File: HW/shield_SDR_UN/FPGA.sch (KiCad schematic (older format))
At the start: 34 parts

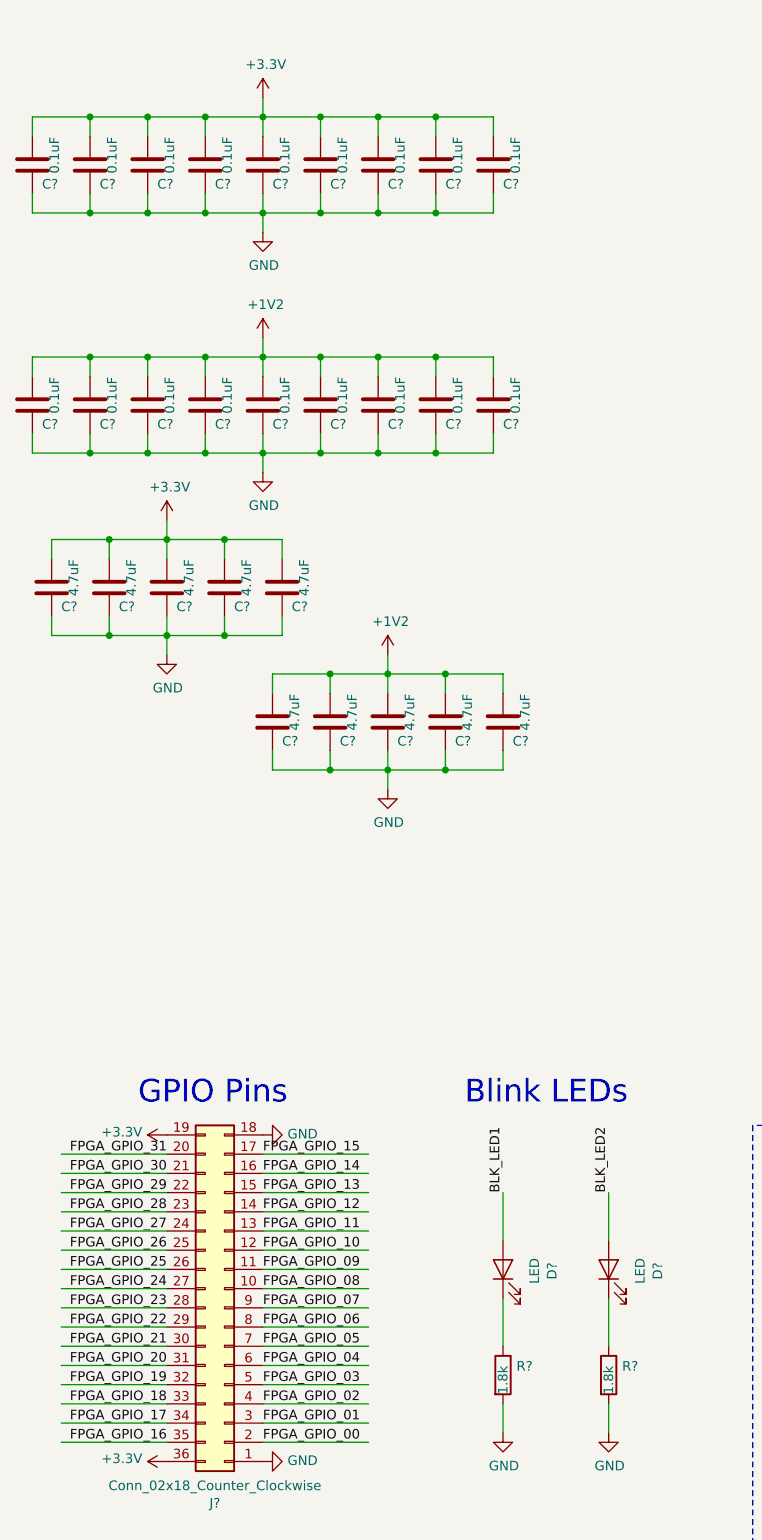
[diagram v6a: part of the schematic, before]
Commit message: algunos footprint
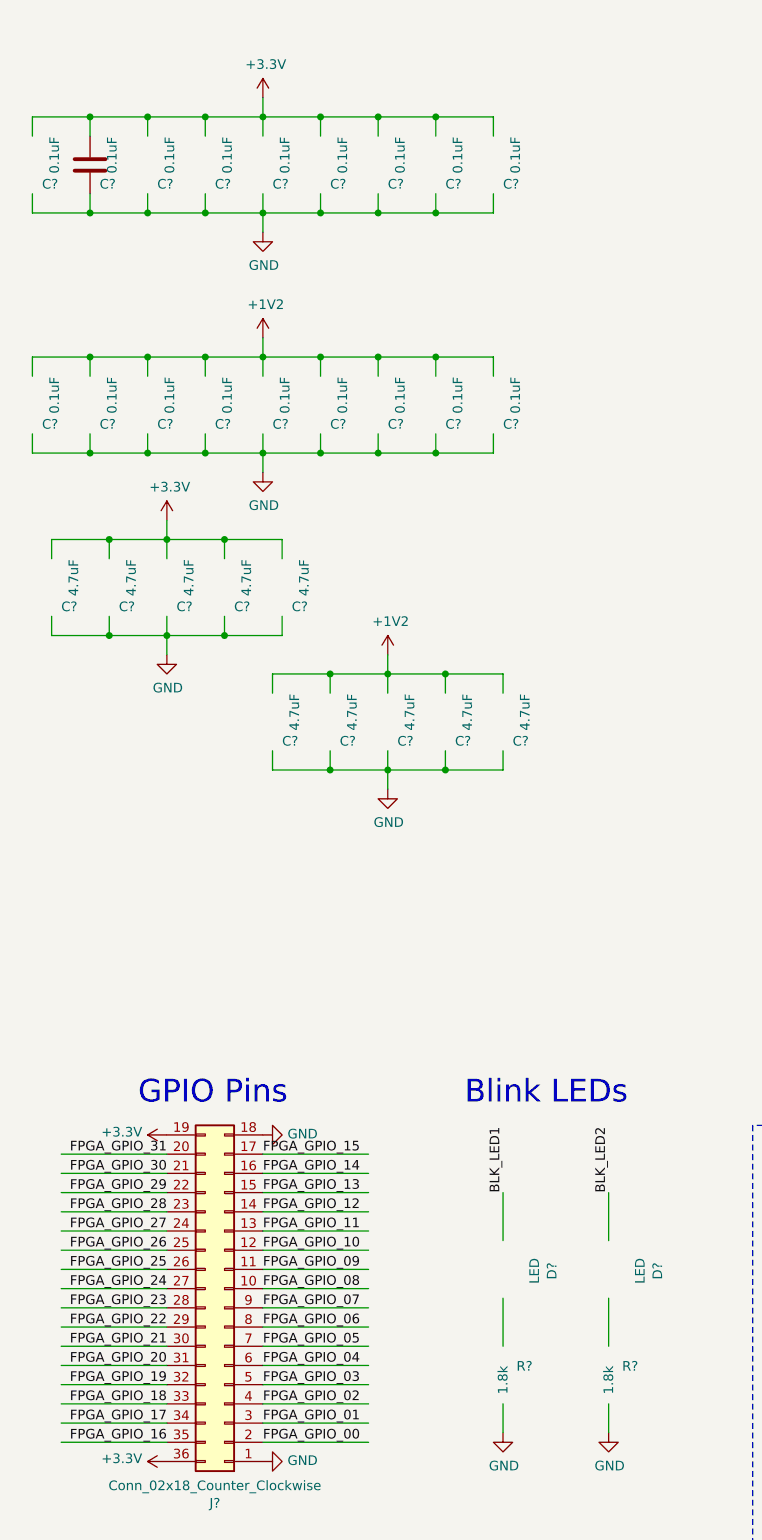
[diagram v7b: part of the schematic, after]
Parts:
- C? (x17): footprint (none) -> Capacitor_SMD:C_0402_1005Metric
- C? (x10): footprint (none) -> Capacitor_SMD:C_0603_1608Metric_Pad1.05x0.95mm_HandSolder
- D? (x2): footprint (none) -> LED_SMD:LED_0805_2012Metric_Pad1.15x1.40mm_HandSolder
- R? (x2): footprint (none) -> Resistor_SMD:R_0603_1608Metric_Pad1.05x0.95mm_HandSolder

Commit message: algunos footprint_v2
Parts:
- added C?: 0.1uF, Capacitor_SMD:C_0402_1005Metric, symbol Device:C
- added D?: LED, LED_SMD:LED_0603_1608Metric_Pad1.05x0.95mm_HandSolder, symbol Device:LED
- added R? (x2): 220, Resistor_SMD:R_0603_1608Metric_Pad1.05x0.95mm_HandSolder, symbol Device:R
- added R?: 4.7k, Resistor_SMD:R_0603_1608Metric_Pad1.05x0.95mm_HandSolder, symbol Device:R
- added SW?: SW_Push, SWITCH_FSM1LPA, symbol FSM1LPTR:FSM1LPTR
- added X?: ASE-xxxMHz, Oscillator:Oscillator_SMD_Abracon_ASE-4Pin_3.2x2.5mm_HandSoldering, symbol Oscillator:ASE-xxxMHz
- U?: value 6SLX9TQG144 -> XC6SLX9-2TQG144C; footprint (none) -> Package_QFP:LQFP-144_20x20mm_P0.5mm; digikey (none) -> 122-1745-ND
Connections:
- net labels added: CLK80MHz, DONE, PROGRAM_B
- wire segments 315 -> 355
- no-connect marks 0 -> 1
